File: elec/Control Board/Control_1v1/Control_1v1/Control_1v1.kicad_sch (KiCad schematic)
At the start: 161 parts, among them J1 DB9_Female_MountingHoles, J10 Conn_02x12_Odd_Even, J11 Screw_Terminal_01x02, J14 Conn_01x10, J2 Conn_01x08, J25 Screw_Terminal_01x02, J26 Conn_01x10, J27 Conn_02x12_Odd_Even, J28 Screw_Terminal_01x02, J29 Conn_01x10, J3 Conn_01x08, J37 Conn_01x04_Pin, J4 Conn_01x08, J5 Conn_01x08, J6 Conn_01x08, J7 Conn_01x10, J8 Conn_02x18_Odd_Even, J9 Conn_01x10, Q601 BSS138

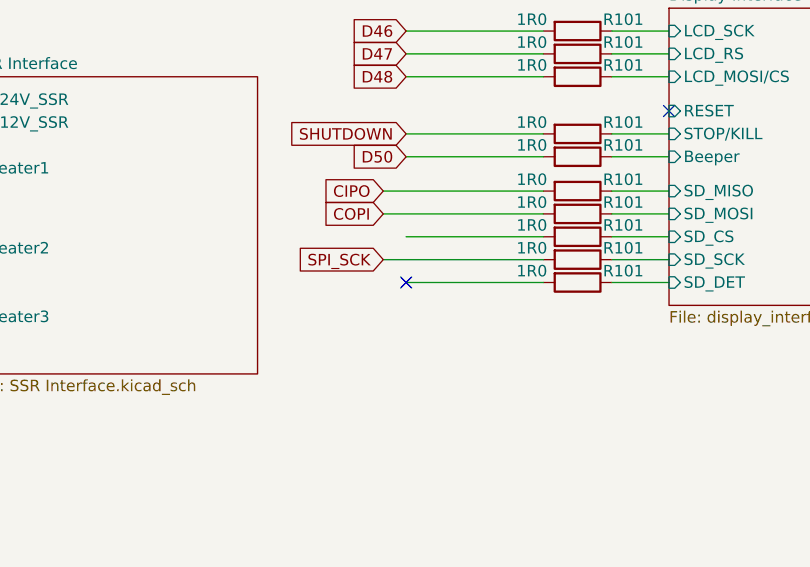
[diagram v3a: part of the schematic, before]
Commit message: Clean up PCB errors and many warnings. PCB has zero DRC errors. Many warnings about silk screen.
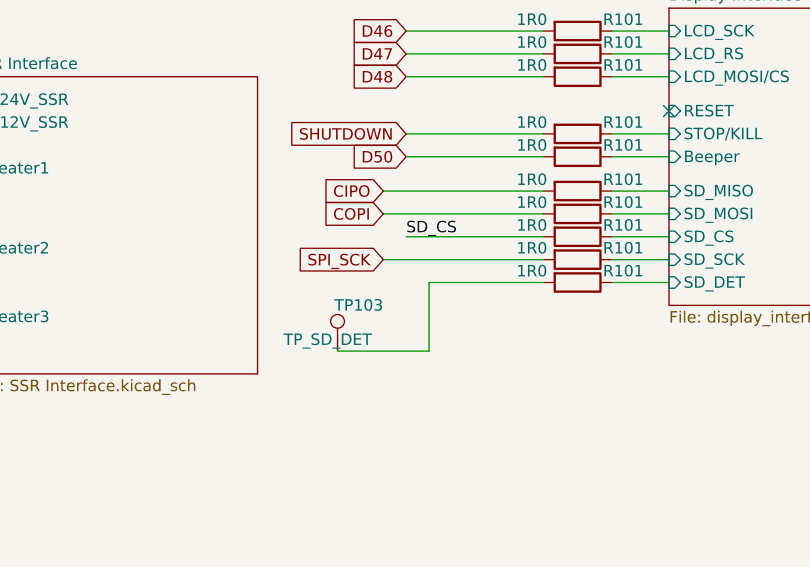
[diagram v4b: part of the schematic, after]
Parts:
- added TP103: TP_SD_DET, TestPoint:TestPoint_Loop_D2.54mm_Drill1.5mm_Beaded, symbol Connector:TestPoint
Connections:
- net SD_CS: now also R101.2
- net at R101.2: now also TP103.1
- no-connect marks 4 -> 3
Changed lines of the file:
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@@
   (no_connect (at 254 54.61))
   (no_connect (at 176.53 175.26))
-  (no_connect (at 425.45 269.24))
   (no_connect (at 454.66 250.19))
   (wire (pts (xy 303.53 142.24) (xy 303.53 147.32))
@@
     (stroke (width 0) (type default))
   )
+  (wire (pts (xy 417.83 276.86) (xy 427.99 276.86))
+    (stroke (width 0) (type default))
+  )
   (wire (pts (xy 212.09 157.48) (xy 212.09 160.02))
     (stroke (width 0) (type default))
@@
     (stroke (width 0) (type default))
   )
+  (wire (pts (xy 427.99 276.86) (xy 427.99 269.24))
+    (stroke (width 0) (type default))
+  )
   (wire (pts (xy 220.98 57.15) (xy 222.25 57.15))
     (stroke (width 0) (type default))
@@
     (stroke (width 0) (type default))
   )
-  (wire (pts (xy 440.69 269.24) (xy 425.45 269.24))
-    (stroke (width 0) (type default))
-  )
   (wire (pts (xy 448.31 269.24) (xy 454.66 269.24))
     (stroke (width 0) (type default))
@@
     (stroke (width 0) (type default))
   )
+  (wire (pts (xy 427.99 269.24) (xy 440.69 269.24))
+    (stroke (width 0) (type default))
+  )
   (wire (pts (xy 443.23 58.42) (xy 433.07 58.42))
     (stroke (width 0) (type default))
@@
     (effects (font (size 1.27 1.27)) (justify right bottom))
   )
+  (label "SD_CS" (at 425.45 264.16 0) (fields_autoplaced)
+    (effects (font (size 1.27 1.27)) (justify left bottom))
+  )
   (label "SD_CS" (at 283.21 71.12 0) (fields_autoplaced)
     (effects (font (size 1.27 1.27)) (justify left bottom))
@@
         )
       )
+    )
+  )
+  (symbol (lib_id "Connector:TestPoint") (at 417.83 276.86 0) (mirror y) (unit 1)
+    (in_bom yes) (on_board yes) (dnp no)
+    (property "Reference" "TP103" (at 422.91 271.78 0)
+      (effects (font (size 1.27 1.27)) (justify left))
+    )
+    (property "Value" "TP_SD_DET" (at 421.64 275.59 0)
+      (effects (font (size 1.27 1.27)) (justify left))
+    )
+    (property "Footprint" "TestPoint:TestPoint_Loop_D2.54mm_Drill1.5mm_Beaded" (at 412.75 276.86 0)
+      (effects (font (size 1.27 1.27)) hide)
+    )
+    (property "Datasheet" "~" (at 412.75 276.86 0)
+      (effects (font (size 1.27 1.27)) hide)
+    )
+    (property "AssemblyType" "HAND" (at 417.83 276.86 0)
+      (effects (font (size 1.27 1.27)) hide)
+    )
+    (property "Cost" "NA" (at 417.83 276.86 0)
+      (effects (font (size 1.27 1.27)) hide)
+    )
+    (pin "1")
+    (instances
+      (project "GeneralPurposeAlarmDevicePCB"
+        (path "/412a327d-1ee3-473e-bc00-1545004b7edf"
+          (reference "TP103") (unit 1)
+        )
+      )
+      (project "Control_1v1"
+        (path "/c68c9deb-8d4d-42f0-adf8-4d3022f4ee59/3ff32a52-b1ed-4756-8661-90a95f721605"
+          (reference "TP1") (unit 1)
+        )
+        (path "/c68c9deb-8d4d-42f0-adf8-4d3022f4ee59"
+          (reference "TP_SD_DET1") (unit 1)
+        )
+      )

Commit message: Still working on a few JLCPCB part numbers for components, headers - sockets.
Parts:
- J37: Cost (none) -> 0.0177; Distributor 1 PN C2905415 -> C6332197
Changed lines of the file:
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@@
+      (effects (font (size 1.27 1.27)) hide)
+    )
+    (property "Description" "50V 10nF NP0 ±5% 0603 Multilayer Ceramic Capacitors MLCC - SMD/SMT ROHS" (at 214.63 242.57 0)
       (effects (font (size 1.27 1.27)) hide)
     )
@@
       (effects (font (size 1.27 1.27)) hide)
     )
-    (property "Datasheet" "KH-2.54FH-1X4P-H8.5.pdf" (at 43.18 297.18 0)
+    (property "Datasheet" "HB-PH3-25414PB2GOP.pdf" (at 43.18 297.18 0)
       (effects (font (size 1.27 1.27)) hide)
     )
@@
       (effects (font (size 1.27 1.27)) hide)
     )
-    (property "Distributor 1 PN" "C2905415" (at 43.18 297.18 0)
-      (effects (font (size 1.27 1.27)) hide)
-    )
+    (property "Distributor 1 PN" "C6332197" (at 43.18 297.18 0)
+      (effects (font (size 1.27 1.27)) hide)
+    )
+    (property "Cost" "0.0177" (at 43.18 297.18 0)
+      (effects (font (size 1.27 1.27)) hide)
+    )
+    (property "Description" "Gold 250V 3A Straight Square Pins 2.54mm 4P 260℃ 6mm -40℃~+105℃ 3mm 2.54mm Brass Black Plugin 1x4P 2.54mm Plugin,P=2.54mm Pin Headers ROHS" (at 43.18 297.18 0)
+      (effects (font (size 1.27 1.27)) hide)
+    )

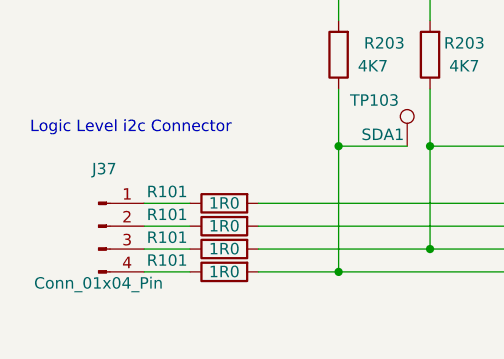
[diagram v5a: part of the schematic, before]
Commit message: Move components away from J35, J36.
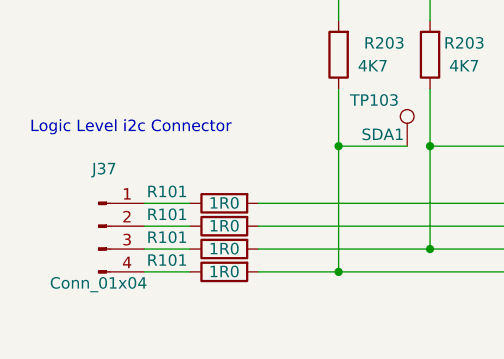
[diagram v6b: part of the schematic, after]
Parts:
- J37: value Conn_01x04_Pin -> Conn_01x04; Cost 0.0177 -> 0.0342; MPN (none) -> HB-PH3-25414PB2GOP; Manufacturer (none) -> Hanbo Electronic
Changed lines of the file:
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@@
       (effects (font (size 1.27 1.27)))
     )
-    (property "Value" "Conn_01x04_Pin" (at 43.18 303.53 0)
+    (property "Value" "Conn_01x04" (at 43.18 303.53 0)
       (effects (font (size 1.27 1.27)))
     )
@@
       (effects (font (size 1.27 1.27)) hide)
     )
-    (property "Cost" "0.0177" (at 43.18 297.18 0)
+    (property "Cost" "0.0342" (at 43.18 297.18 0)
       (effects (font (size 1.27 1.27)) hide)
     )
-    (property "Description" "Gold 250V 3A Straight Square Pins 2.54mm 4P 260℃ 6mm -40℃~+105℃ 3mm 2.54mm Brass Black Plugin 1x4P 2.54mm Plugin,P=2.54mm Pin Headers ROHS" (at 43.18 297.18 0)
+    (property "Description" "2.54mm Plugin 3A 4P -40℃~+105℃ Straight 1x4P 8.5mm Top Square Holes Plugin,P=2.54mm Female Headers ROHS" (at 43.18 297.18 0)
       (effects (font (size 1.27 1.27)) hide)
     )
+    (property "MPN" "HB-PH3-25414PB2GOP" (at 43.18 297.18 0)
+      (effects (font (size 1.27 1.27)) hide)
+    )
+    (property "Manufacturer" "Hanbo Electronic" (at 43.18 297.18 0)
+      (effects (font (size 1.27 1.27)) hide)
+    )

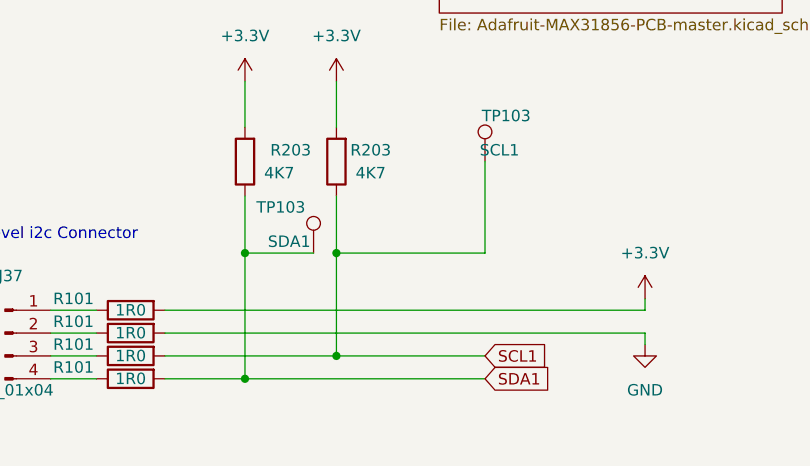
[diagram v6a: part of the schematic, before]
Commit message: Add another gnd test point.
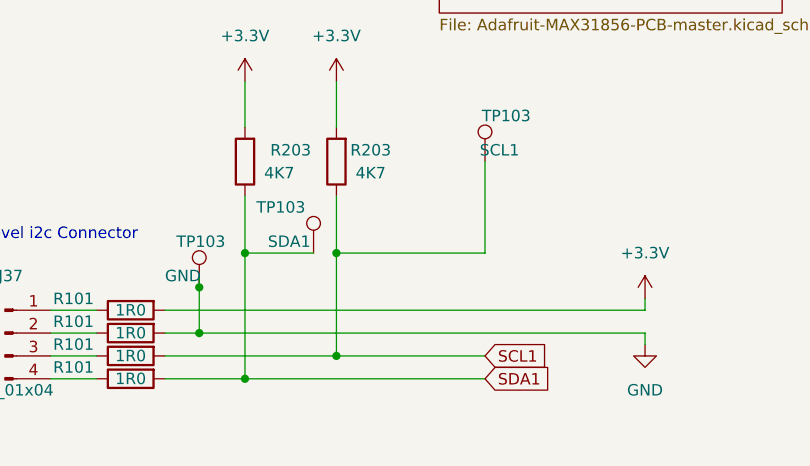
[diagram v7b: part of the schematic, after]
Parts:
- added TP103: GND, TestPoint:TestPoint_Loop_D2.54mm_Drill1.5mm_Beaded, symbol Connector:TestPoint
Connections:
- net GND: now also TP103.1
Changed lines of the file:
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@@
   (junction (at 175.26 66.04) (diameter 0) (color 0 0 0 0)
   )
+  (junction (at 64.77 297.18) (diameter 0) (color 0 0 0 0)
+  )
   (junction (at 223.52 234.95) (diameter 0) (color 0 0 0 0)
   )
@@
   (junction (at 201.93 71.12) (diameter 0) (color 0 0 0 0)
   )
+  (junction (at 64.77 292.1) (diameter 0) (color 0 0 0 0)
+  )
   (junction (at 190.5 165.1) (diameter 0) (color 0 0 0 0)
   )
@@
     (stroke (width 0) (type default))
   )
-  (wire (pts (xy 60.96 297.18) (xy 114.3 297.18))
+  (wire (pts (xy 60.96 297.18) (xy 64.77 297.18))
     (stroke (width 0) (type default))
   )
@@
     (stroke (width 0) (type default))
   )
+  (wire (pts (xy 64.77 292.1) (xy 64.77 297.18))
+    (stroke (width 0) (type default))
+  )
   (wire (pts (xy 355.6 196.85) (xy 358.14 196.85))
     (stroke (width 0) (type default))
@@
     (stroke (width 0) (type default))
   )
+  (wire (pts (xy 64.77 290.83) (xy 64.77 292.1))
+    (stroke (width 0) (type default))
+  )
   (wire (pts (xy 172.72 152.4) (xy 181.61 152.4))
     (stroke (width 0) (type default))
@@
     (stroke (width 0) (type default))
   )
+  (wire (pts (xy 64.77 297.18) (xy 114.3 297.18))
+    (stroke (width 0) (type default))
+  )
   (wire (pts (xy 453.39 29.21) (xy 461.01 29.21))
     (stroke (width 0) (type default))
@@
         )
       )
+    )
+  )
+  (symbol (lib_id "Connector:TestPoint") (at 64.77 292.1 0) (unit 1)
+    (in_bom yes) (on_board yes) (dnp no)
+    (property "Reference" "TP103" (at 62.23 287.02 0)
+      (effects (font (size 1.27 1.27)) (justify left))
+    )
+    (property "Value" "GND" (at 60.96 290.83 0)
+      (effects (font (size 1.27 1.27)) (justify left))
+    )
+    (property "Footprint" "TestPoint:TestPoint_Loop_D2.54mm_Drill1.5mm_Beaded" (at 69.85 292.1 0)
+      (effects (font (size 1.27 1.27)) hide)
+    )
+    (property "Datasheet" "~" (at 69.85 292.1 0)
+      (effects (font (size 1.27 1.27)) hide)
+    )
+    (property "AssemblyType" "HAND" (at 64.77 292.1 0)
+      (effects (font (size 1.27 1.27)) hide)
+    )
+    (property "Cost" "NA" (at 64.77 292.1 0)
+      (effects (font (size 1.27 1.27)) hide)
+    )
+    (pin "1")
+    (instances
+      (project "GeneralPurposeAlarmDevicePCB"
+        (path "/412a327d-1ee3-473e-bc00-1545004b7edf"
+          (reference "TP103") (unit 1)
+        )
+      )
+      (project "Control_1v1"
+        (path "/c68c9deb-8d4d-42f0-adf8-4d3022f4ee59/3ff32a52-b1ed-4756-8661-90a95f721605"
+          (reference "TP1") (unit 1)
+        )
+        (path "/c68c9deb-8d4d-42f0-adf8-4d3022f4ee59"
+          (reference "TP21") (unit 1)
+        )
+      )

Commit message: Add JLCPCB order files after fixing out of stock components.
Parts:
- R203: Distributor 1 PN C269713 -> C23162; Manufacturer TyoHM -> UNI-ROYAL(Uniroyal Elec)
- R203: Distributor 1 PN C269713 -> C23162; MPN RMC 0603 4K7 F N -> 0603WAF4701T5E; Manufacturer TyoHM -> UNI-ROYAL(Uniroyal Elec)
- S101: Distributor 1 PN C13828 -> C428628
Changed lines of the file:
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@@
       (effects (font (size 1.27 1.27)) hide)
     )
-    (property "Distributor 1 PN" "C269713" (at 393.7 48.26 90)
+    (property "Distributor 1 PN" "C23162" (at 393.7 48.26 90)
       (effects (font (size 1.27 1.27)) hide)
     )
-    (property "Manufacturer" "TyoHM" (at 393.7 48.26 90)
+    (property "Manufacturer" "UNI-ROYAL(Uniroyal Elec)" (at 393.7 48.26 90)
       (effects (font (size 1.27 1.27)) hide)
     )
@@
       (effects (font (size 1.27 1.27)) hide)
     )
-    (property "Description" "1W ±1% 4.7kΩ 0603 Chip Resistor - Surface Mount ROHS" (at 393.7 48.26 0)
+    (property "Description" "100mW Thick Film Resistors ±100ppm/℃ ±1% 4.7kΩ 0603 Chip Resistor - Surface Mount ROHS" (at 393.7 48.26 0)
       (effects (font (size 1.27 1.27)) hide)
     )
@@
       (effects (font (size 1.27 1.27)) hide)
     )
-    (property "Distributor 1 PN" "C269713" (at 426.72 207.01 90)
+    (property "Distributor 1 PN" "C23162" (at 426.72 207.01 90)
       (effects (font (size 1.27 1.27)) hide)
     )
-    (property "Manufacturer" "TyoHM" (at 426.72 207.01 90)
+    (property "Manufacturer" "UNI-ROYAL(Uniroyal Elec)" (at 426.72 207.01 90)
       (effects (font (size 1.27 1.27)) hide)
     )
@@
       (effects (font (size 1.27 1.27)) hide)
     )
-    (property "Description" "1W ±1% 4.7kΩ 0603 Chip Resistor - Surface Mount ROHS" (at 426.72 207.01 0)
+    (property "Description" "100mW Thick Film Resistors ±100ppm/℃ ±1% 4.7kΩ 0603 Chip Resistor - Surface Mount ROHS" (at 426.72 207.01 0)
       (effects (font (size 1.27 1.27)) hide)
     )
@@
       (effects (font (size 1.27 1.27)) hide)
     )
-    (property "Distributor 1 PN" "C269713" (at 161.29 41.91 90)
+    (property "Distributor 1 PN" "C23162" (at 161.29 41.91 90)
       (effects (font (size 1.27 1.27)) hide)
     )
-    (property "Manufacturer" "TyoHM" (at 161.29 41.91 90)
+    (property "Manufacturer" "UNI-ROYAL(Uniroyal Elec)" (at 161.29 41.91 90)
       (effects (font (size 1.27 1.27)) hide)
     )
-    (property "MPN" "RMC 0603 4K7 F N" (at 161.29 41.91 90)
+    (property "MPN" "0603WAF4701T5E" (at 161.29 41.91 90)
       (effects (font (size 1.27 1.27)) hide)
     )
-    (property "Description" "1W ±1% 4.7kΩ 0603 Chip Resistor - Surface Mount ROHS" (at 161.29 41.91 0)
+    (property "Description" "100mW Thick Film Resistors ±100ppm/℃ ±1% 4.7kΩ 0603 Chip Resistor - Surface Mount ROHS" (at 161.29 41.91 0)
       (effects (font (size 1.27 1.27)) hide)
     )
@@
       (effects (font (size 1.27 1.27)) hide)
     )
-    (property "Distributor 1 PN" "C13828" (at 194.31 46.99 0)
+    (property "Distributor 1 PN" "C428628" (at 194.31 46.99 0)
       (effects (font (size 1.27 1.27)) hide)
     )
@@
       (effects (font (size 1.27 1.27)) hide)
     )
-    (property "Distributor 1 PN" "C13828" (at 278.13 201.93 0)
+    (property "Distributor 1 PN" "C428628" (at 278.13 201.93 0)
       (effects (font (size 1.27 1.27)) hide)
     )
@@
       (effects (font (size 1.27 1.27)) hide)
     )
-    (property "Distributor 1 PN" "C269713" (at 393.7 119.38 90)
+    (property "Distributor 1 PN" "C23162" (at 393.7 119.38 90)
       (effects (font (size 1.27 1.27)) hide)
     )
-    (property "Manufacturer" "TyoHM" (at 393.7 119.38 90)
+    (property "Manufacturer" "UNI-ROYAL(Uniroyal Elec)" (at 393.7 119.38 90)
       (effects (font (size 1.27 1.27)) hide)
     )
@@
       (effects (font (size 1.27 1.27)) hide)
     )
-    (property "Description" "1W ±1% 4.7kΩ 0603 Chip Resistor - Surface Mount ROHS" (at 393.7 119.38 0)
+    (property "Description" "100mW Thick Film Resistors ±100ppm/℃ ±1% 4.7kΩ 0603 Chip Resistor - Surface Mount ROHS" (at 393.7 119.38 0)
       (effects (font (size 1.27 1.27)) hide)
     )
@@
       (effects (font (size 1.27 1.27)) hide)
     )
-    (property "Distributor 1 PN" "C269713" (at 69.85 278.13 90)
+    (property "Distributor 1 PN" "C23162" (at 69.85 278.13 90)
       (effects (font (size 1.27 1.27)) hide)
     )
-    (property "Manufacturer" "TyoHM" (at 69.85 278.13 90)
+    (property "Manufacturer" "UNI-ROYAL(Uniroyal Elec)" (at 69.85 278.13 90)
       (effects (font (size 1.27 1.27)) hide)
     )
@@
       (effects (font (size 1.27 1.27)) hide)
     )
-    (property "Description" "1W ±1% 4.7kΩ 0603 Chip Resistor - Surface Mount ROHS" (at 69.85 278.13 0)
+    (property "Description" "100mW Thick Film Resistors ±100ppm/℃ ±1% 4.7kΩ 0603 Chip Resistor - Surface Mount ROHS" (at 69.85 278.13 0)
       (effects (font (size 1.27 1.27)) hide)
     )
@@
       (effects (font (size 1.27 1.27)) hide)
     )
-    (property "Distributor 1 PN" "C269713" (at 80.01 278.13 90)
+    (property "Distributor 1 PN" "C23162" (at 80.01 278.13 90)
       (effects (font (size 1.27 1.27)) hide)
     )
-    (property "Manufacturer" "TyoHM" (at 80.01 278.13 90)
+    (property "Manufacturer" "UNI-ROYAL(Uniroyal Elec)" (at 80.01 278.13 90)
       (effects (font (size 1.27 1.27)) hide)
     )
@@
       (effects (font (size 1.27 1.27)) hide)
     )
-    (property "Description" "1W ±1% 4.7kΩ 0603 Chip Resistor - Surface Mount ROHS" (at 80.01 278.13 0)
+    (property "Description" "100mW Thick Film Resistors ±100ppm/℃ ±1% 4.7kΩ 0603 Chip Resistor - Surface Mount ROHS" (at 80.01 278.13 0)
       (effects (font (size 1.27 1.27)) hide)
     )
@@
       (effects (font (size 1.27 1.27)) hide)
     )
-    (property "Distributor 1 PN" "C269713" (at 171.45 41.91 90)
+    (property "Distributor 1 PN" "C23162" (at 171.45 41.91 90)
       (effects (font (size 1.27 1.27)) hide)
     )
-    (property "Manufacturer" "TyoHM" (at 171.45 41.91 90)
+    (property "Manufacturer" "UNI-ROYAL(Uniroyal Elec)" (at 171.45 41.91 90)
       (effects (font (size 1.27 1.27)) hide)
     )
@@
       (effects (font (size 1.27 1.27)) hide)
     )
-    (property "Description" "1W ±1% 4.7kΩ 0603 Chip Resistor - Surface Mount ROHS" (at 171.45 41.91 0)
+    (property "Description" "100mW Thick Film Resistors ±100ppm/℃ ±1% 4.7kΩ 0603 Chip Resistor - Surface Mount ROHS" (at 171.45 41.91 0)
       (effects (font (size 1.27 1.27)) hide)
     )
